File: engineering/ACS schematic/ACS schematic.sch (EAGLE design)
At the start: 4 parts

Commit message: schematics & engineering
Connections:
- net N$6 renamed W1
- net N$8 renamed W0
- removed net N$4: B1.GND@0, MCP41010.B0, MCP41010.B1, MCP41010.GND
- removed net N$5: B1.5V, MCP41010.A0, MCP41010.A1, MCP41010.VCC
- net GND: now also B1.GND@0, MCP41010.B0, MCP41010.B1, MCP41010.GND
- net VCC: now also B1.5V, MCP41010.A0, MCP41010.A1, MCP41010.VCC
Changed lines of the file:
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@@
 <plain>
 <text x="68.58" y="15.24" size="1.778" layer="91">MCP41010</text>
-<text x="30.48" y="10.16" size="1.778" layer="101">MC</text>
-<text x="30.48" y="0" size="1.778" layer="101">MC</text>
-<polygon width="0.1524" layer="208" spacing="76.2" pour="hatch">
-<vertex x="27.94" y="12.7"/>
-<vertex x="27.94" y="7.62"/>
-<vertex x="35.56" y="7.62"/>
-<vertex x="35.56" y="12.7"/>
-</polygon>
-<polygon width="0.1524" layer="208" spacing="76.2" pour="hatch">
-<vertex x="27.94" y="2.54"/>
-<vertex x="27.94" y="-2.54"/>
-<vertex x="35.56" y="-2.54"/>
-<vertex x="35.56" y="2.54"/>
-</polygon>
+<text x="30.48" y="10.16" size="1.778" layer="91">MC</text>
+<text x="30.48" y="0" size="1.778" layer="91">MC</text>
 </plain>
 <instances>
 <instance part="B1" gate="G$1" x="27.94" y="48.26"/>
-<instance part="MCP41010" gate="G$1" x="73.66" y="50.8">
-<attribute name="MCP41010" x="73.66" y="50.8" size="1.778" layer="96" display="off"/>
+<instance part="MCP41010" gate="G$1" x="73.66" y="48.26">
+<attribute name="MCP41010" x="73.66" y="48.26" size="1.778" layer="96" display="off"/>
 </instance>
 <instance part="SUPPLY1" gate="G$1" x="7.62" y="40.64"/>
@@
 </busses>
 <nets>
-<net name="N$5" class="0">
-<segment>
-<wire x1="10.16" y1="71.12" x2="53.34" y2="71.12" width="0.1524" layer="91"/>
-<pinref part="MCP41010" gate="G$1" pin="VCC"/>
-<junction x="63.5" y="68.58"/>
-<wire x1="53.34" y1="71.12" x2="58.42" y2="71.12" width="0.1524" layer="91"/>
-<wire x1="58.42" y1="71.12" x2="63.5" y2="71.12" width="0.1524" layer="91"/>
-<wire x1="63.5" y1="71.12" x2="63.5" y2="68.58" width="0.1524" layer="91"/>
-<pinref part="MCP41010" gate="G$1" pin="A1"/>
-<wire x1="63.5" y1="50.8" x2="53.34" y2="60.96" width="0.1524" layer="91"/>
-<wire x1="53.34" y1="60.96" x2="53.34" y2="71.12" width="0.1524" layer="91"/>
-<junction x="53.34" y="71.12"/>
-<pinref part="MCP41010" gate="G$1" pin="A0"/>
-<wire x1="63.5" y1="60.96" x2="58.42" y2="66.04" width="0.1524" layer="91"/>
-<wire x1="58.42" y1="66.04" x2="58.42" y2="71.12" width="0.1524" layer="91"/>
-<junction x="58.42" y="71.12"/>
-<pinref part="B1" gate="G$1" pin="5V"/>
-<wire x1="15.24" y1="38.1" x2="10.16" y2="38.1" width="0.1524" layer="91"/>
-<wire x1="10.16" y1="38.1" x2="10.16" y2="71.12" width="0.1524" layer="91"/>
-</segment>
-</net>
-<net name="N$4" class="0">
-<segment>
-<pinref part="MCP41010" gate="G$1" pin="GND"/>
-<wire x1="63.5" y1="20.32" x2="60.96" y2="20.32" width="0.1524" layer="91"/>
-<wire x1="60.96" y1="20.32" x2="55.88" y2="20.32" width="0.1524" layer="91"/>
-<pinref part="MCP41010" gate="G$1" pin="B0"/>
-<wire x1="63.5" y1="55.88" x2="60.96" y2="53.34" width="0.1524" layer="91"/>
-<wire x1="60.96" y1="53.34" x2="60.96" y2="20.32" width="0.1524" layer="91"/>
-<junction x="60.96" y="20.32"/>
-<pinref part="MCP41010" gate="G$1" pin="B1"/>
-<wire x1="63.5" y1="45.72" x2="55.88" y2="38.1" width="0.1524" layer="91"/>
-<wire x1="55.88" y1="38.1" x2="55.88" y2="20.32" width="0.1524" layer="91"/>
-<pinref part="B1" gate="G$1" pin="GND@0"/>
-<wire x1="15.24" y1="25.4" x2="15.24" y2="20.32" width="0.1524" layer="91"/>
-<wire x1="15.24" y1="20.32" x2="55.88" y2="20.32" width="0.1524" layer="91"/>
-<junction x="55.88" y="20.32"/>
-</segment>
-</net>
 <net name="N$1" class="0">
 <segment>
+<pinref part="B1" gate="G$1" pin="D13"/>
+<wire x1="50.8" y1="38.1" x2="50.8" y2="30.48" width="0.1524" layer="91"/>
+<wire x1="50.8" y1="30.48" x2="40.64" y2="30.48" width="0.1524" layer="91"/>
 <pinref part="MCP41010" gate="G$1" pin="SCK"/>
-<wire x1="63.5" y1="40.64" x2="50.8" y2="40.64" width="0.1524" layer="91"/>
-<wire x1="50.8" y1="40.64" x2="50.8" y2="30.48" width="0.1524" layer="91"/>
-<pinref part="B1" gate="G$1" pin="D13"/>
-<wire x1="50.8" y1="30.48" x2="40.64" y2="30.48" width="0.1524" layer="91"/>
-</segment>
-</net>
-<net name="N$2" class="0">
-<segment>
-<pinref part="MCP41010" gate="G$1" pin="DI"/>
-<pinref part="B1" gate="G$1" pin="*D11"/>
-<wire x1="63.5" y1="38.1" x2="48.26" y2="38.1" width="0.1524" layer="91"/>
-<wire x1="48.26" y1="38.1" x2="40.64" y2="35.56" width="0.1524" layer="91"/>
-</segment>
-</net>
-<net name="N$3" class="0">
-<segment>
-<pinref part="MCP41010" gate="G$1" pin="DO"/>
-<pinref part="B1" gate="G$1" pin="D12"/>
-<wire x1="63.5" y1="35.56" x2="48.26" y2="35.56" width="0.1524" layer="91"/>
-<wire x1="48.26" y1="35.56" x2="40.64" y2="33.02" width="0.1524" layer="91"/>
+<wire x1="63.5" y1="38.1" x2="50.8" y2="38.1" width="0.1524" layer="91"/>
 </segment>
 </net>
@@
 <wire x1="7.62" y1="40.64" x2="15.24" y2="40.64" width="0.1524" layer="91"/>
 </segment>
+<segment>
+<wire x1="10.16" y1="71.12" x2="53.34" y2="71.12" width="0.1524" layer="91"/>
+<pinref part="MCP41010" gate="G$1" pin="VCC"/>
+<junction x="63.5" y="66.04"/>
+<wire x1="53.34" y1="71.12" x2="58.42" y2="71.12" width="0.1524" layer="91"/>
+<wire x1="58.42" y1="71.12" x2="63.5" y2="71.12" width="0.1524" layer="91"/>
+<wire x1="63.5" y1="71.12" x2="63.5" y2="66.04" width="0.1524" layer="91"/>
+<pinref part="MCP41010" gate="G$1" pin="A1"/>
+<wire x1="63.5" y1="48.26" x2="53.34" y2="60.96" width="0.1524" layer="91"/>
+<wire x1="53.34" y1="60.96" x2="53.34" y2="71.12" width="0.1524" layer="91"/>
+<junction x="53.34" y="71.12"/>
+<pinref part="MCP41010" gate="G$1" pin="A0"/>
+<wire x1="63.5" y1="58.42" x2="58.42" y2="66.04" width="0.1524" layer="91"/>
+<wire x1="58.42" y1="66.04" x2="58.42" y2="71.12" width="0.1524" layer="91"/>
+<junction x="58.42" y="71.12"/>
+<pinref part="B1" gate="G$1" pin="5V"/>
+<wire x1="15.24" y1="38.1" x2="10.16" y2="38.1" width="0.1524" layer="91"/>
+<wire x1="10.16" y1="38.1" x2="10.16" y2="71.12" width="0.1524" layer="91"/>
+<label x="27.94" y="71.12" size="1.778" layer="95"/>
+</segment>
 </net>
 <net name="GND" class="0">
@@
 <wire x1="7.62" y1="30.48" x2="15.24" y2="30.48" width="0.1524" layer="91"/>
 </segment>
+<segment>
+<wire x1="60.96" y1="20.32" x2="55.88" y2="20.32" width="0.1524" layer="91"/>
+<pinref part="MCP41010" gate="G$1" pin="B0"/>
+<wire x1="63.5" y1="53.34" x2="60.96" y2="53.34" width="0.1524" layer="91"/>
+<wire x1="60.96" y1="53.34" x2="60.96" y2="20.32" width="0.1524" layer="91"/>
+<wire x1="55.88" y1="43.18" x2="55.88" y2="20.32" width="0.1524" layer="91"/>
+<pinref part="B1" gate="G$1" pin="GND@0"/>
+<wire x1="15.24" y1="25.4" x2="15.24" y2="20.32" width="0.1524" layer="91"/>
+<wire x1="15.24" y1="20.32" x2="55.88" y2="20.32" width="0.1524" layer="91"/>
+<junction x="55.88" y="20.32"/>
+<pinref part="MCP41010" gate="G$1" pin="GND"/>
+<wire x1="63.5" y1="17.78" x2="60.96" y2="17.78" width="0.1524" layer="91"/>
+<wire x1="60.96" y1="17.78" x2="60.96" y2="20.32" width="0.1524" layer="91"/>
+<junction x="60.96" y="20.32"/>
+<pinref part="MCP41010" gate="G$1" pin="B1"/>
+<wire x1="63.5" y1="43.18" x2="55.88" y2="43.18" width="0.1524" layer="91"/>
+<label x="60.96" y="15.24" size="1.778" layer="95"/>
+</segment>
 </net>
-<net name="N$8" class="0">
+<net name="W0" class="0">
 <segment>
-<pinref part="MCP41010" gate="G$1" pin="W0"/>
-<wire x1="63.5" y1="58.42" x2="58.42" y2="58.42" width="0.1524" layer="91"/>
 <pinref part="S2" gate="1" pin="P"/>
 <wire x1="53.34" y1="12.7" x2="58.42" y2="12.7" width="0.1524" layer="91"/>
-<wire x1="58.42" y1="12.7" x2="58.42" y2="58.42" width="0.1524" layer="91"/>
+<pinref part="MCP41010" gate="G$1" pin="W0"/>
+<wire x1="63.5" y1="55.88" x2="58.42" y2="55.88" width="0.1524" layer="91"/>
+<wire x1="58.42" y1="55.88" x2="58.42" y2="12.7" width="0.1524" layer="91"/>
+<label x="55.88" y="12.7" size="1.778" layer="95"/>
 </segment>
 </net>
-<net name="N$6" class="0">
+<net name="W1" class="0">
 <segment>
+<pinref part="S1" gate="1" pin="P"/>
 <pinref part="MCP41010" gate="G$1" pin="W1"/>
-<wire x1="63.5" y1="48.26" x2="53.34" y2="48.26" width="0.1524" layer="91"/>
-<pinref part="S1" gate="1" pin="P"/>
-<wire x1="53.34" y1="48.26" x2="53.34" y2="2.54" width="0.1524" layer="91"/>
+<wire x1="53.34" y1="45.72" x2="53.34" y2="2.54" width="0.1524" layer="91"/>
+<wire x1="63.5" y1="45.72" x2="53.34" y2="45.72" width="0.1524" layer="91"/>
+<label x="53.34" y="5.08" size="1.778" layer="95"/>
 </segment>
 </net>
@@
 </segment>
 </net>
+<net name="N$2" class="0">
+<segment>
+<pinref part="MCP41010" gate="G$1" pin="DI"/>
+<pinref part="B1" gate="G$1" pin="*D11"/>
+<wire x1="63.5" y1="35.56" x2="40.64" y2="35.56" width="0.1524" layer="91"/>
+</segment>
+</net>
+<net name="N$3" class="0">
+<segment>
+<pinref part="MCP41010" gate="G$1" pin="DO"/>
+<pinref part="B1" gate="G$1" pin="D12"/>
+<wire x1="63.5" y1="33.02" x2="40.64" y2="33.02" width="0.1524" layer="91"/>
+</segment>
+</net>

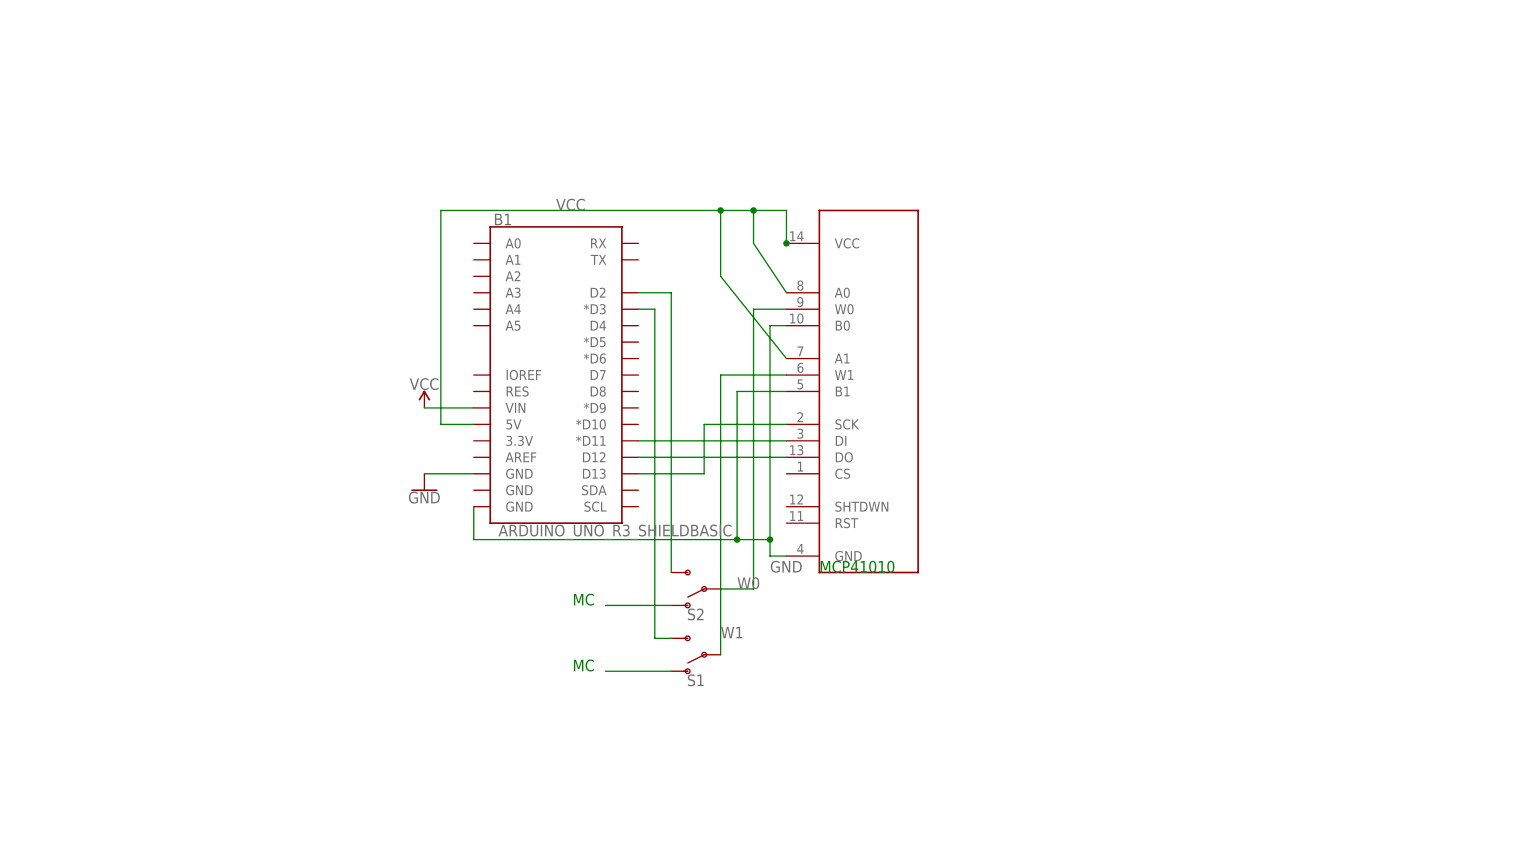
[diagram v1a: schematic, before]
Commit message: recorder added, steering training changes, config stuff added, other small changes
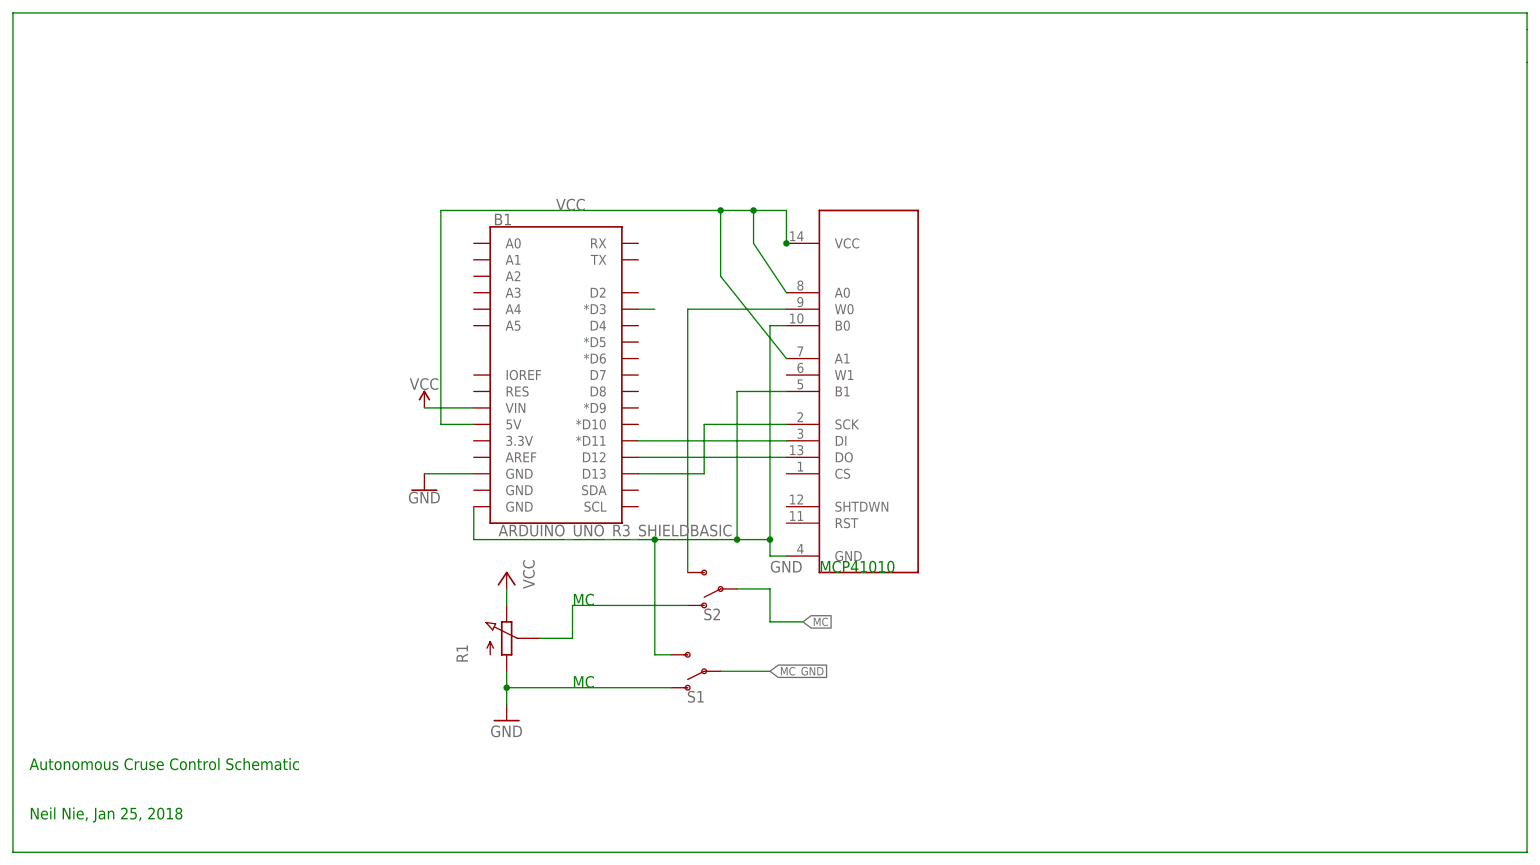
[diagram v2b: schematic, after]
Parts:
- added R1: (no value), pot-vitrohm:PC25
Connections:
- removed net N$11: S1.O
- removed net N$7: B1.D2, S2.S
- removed net W1: MCP41010.W1, S1.P
- new net MC: S2.P
- new net MC_GND: S1.P
- net GND: now also R1.A, S1.O, S1.S
- net N$10: now also R1.S
- net N$9: no longer S1.S
- net VCC: now also R1.E
- net W0: now also S2.S; no longer S2.P
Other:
- note added: "Autonomous Cruse Control Schematic"
- note added: "Neil Nie, Jan 25, 2018"
- moved on the sheet: S1, S2
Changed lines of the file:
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@@
 <?xml version="1.0" encoding="utf-8"?>
 <!DOCTYPE eagle SYSTEM "eagle.dtd">
-<eagle version="8.5.2">
+<eagle version="8.6.0">
 <drawing>
 <settings>
@@
 <part name="S1" library="SparkFun-Switches" library_urn="urn:adsk.eagle:library:535" deviceset="SWITCH-SPDT" device="-PTH-11.6X4.0MM" package3d_urn="urn:adsk.eagle:package:40177/1"/>
 <part name="S2" library="SparkFun-Switches" library_urn="urn:adsk.eagle:library:535" deviceset="SWITCH-SPDT" device="-PTH-11.6X4.0MM" package3d_urn="urn:adsk.eagle:package:40177/1"/>
+<part name="R1" library="pot-vitrohm" library_urn="urn:adsk.eagle:library:329" deviceset="PC25" device="" package3d_urn="urn:adsk.eagle:package:22616/1"/>
+<part name="GND2" library="supply1" library_urn="urn:adsk.eagle:library:371" deviceset="GND" device=""/>
+<part name="P+1" library="supply1" library_urn="urn:adsk.eagle:library:371" deviceset="VCC" device=""/>
 </parts>
 <sheets>
@@
 <text x="68.58" y="15.24" size="1.778" layer="91">MCP41010</text>
 <text x="30.48" y="10.16" size="1.778" layer="91">MC</text>
-<text x="30.48" y="0" size="1.778" layer="91">MC</text>
+<text x="30.48" y="-2.54" size="1.778" layer="91">MC</text>
+<text x="-53.34" y="-15.24" size="1.778" layer="91">Autonomous Cruse Control Schematic</text>
+<text x="-53.34" y="-22.86" size="1.778" layer="91">Neil Nie, Jan 25, 2018</text>
 </plain>
 <instances>
@@
 <instance part="SUPPLY1" gate="G$1" x="7.62" y="40.64"/>
 <instance part="GND1" gate="1" x="7.62" y="27.94"/>
-<instance part="S1" gate="1" x="50.8" y="2.54" rot="R180"/>
-<instance part="S2" gate="1" x="50.8" y="12.7" rot="R180"/>
+<instance part="S1" gate="1" x="50.8" y="0" rot="R180"/>
+<instance part="S2" gate="1" x="53.34" y="12.7" rot="R180"/>
+<instance part="R1" gate="G" x="20.32" y="5.08"/>
+<instance part="GND2" gate="1" x="20.32" y="-7.62"/>
+<instance part="P+1" gate="VCC" x="20.32" y="15.24" rot="MR0"/>
 </instances>
 <busses>
@@
 <label x="27.94" y="71.12" size="1.778" layer="95"/>
 </segment>
+<segment>
+<pinref part="R1" gate="G" pin="E"/>
+<pinref part="P+1" gate="VCC" pin="VCC"/>
+<wire x1="20.32" y1="10.16" x2="20.32" y2="12.7" width="0.1524" layer="91"/>
+</segment>
 </net>
 <net name="GND" class="0">
@@
 <pinref part="B1" gate="G$1" pin="GND@0"/>
 <wire x1="15.24" y1="25.4" x2="15.24" y2="20.32" width="0.1524" layer="91"/>
-<wire x1="15.24" y1="20.32" x2="55.88" y2="20.32" width="0.1524" layer="91"/>
+<wire x1="15.24" y1="20.32" x2="43.18" y2="20.32" width="0.1524" layer="91"/>
 <junction x="55.88" y="20.32"/>
 <pinref part="MCP41010" gate="G$1" pin="GND"/>
+<wire x1="43.18" y1="20.32" x2="55.88" y2="20.32" width="0.1524" layer="91"/>
 <wire x1="63.5" y1="17.78" x2="60.96" y2="17.78" width="0.1524" layer="91"/>
 <wire x1="60.96" y1="17.78" x2="60.96" y2="20.32" width="0.1524" layer="91"/>
@@
 <wire x1="63.5" y1="43.18" x2="55.88" y2="43.18" width="0.1524" layer="91"/>
 <label x="60.96" y="15.24" size="1.778" layer="95"/>
+<pinref part="S1" gate="1" pin="S"/>
+<wire x1="45.72" y1="2.54" x2="43.18" y2="2.54" width="0.1524" layer="91"/>
+<wire x1="43.18" y1="2.54" x2="43.18" y2="20.32" width="0.1524" layer="91"/>
+<junction x="43.18" y="20.32"/>
+</segment>
+<segment>
+<pinref part="R1" gate="G" pin="A"/>
+<pinref part="GND2" gate="1" pin="GND"/>
+<wire x1="20.32" y1="0" x2="20.32" y2="-2.54" width="0.1524" layer="91"/>
+<pinref part="S1" gate="1" pin="O"/>
+<wire x1="20.32" y1="-2.54" x2="20.32" y2="-5.08" width="0.1524" layer="91"/>
+<wire x1="45.72" y1="-2.54" x2="20.32" y2="-2.54" width="0.1524" layer="91"/>
+<junction x="20.32" y="-2.54"/>
 </segment>
 </net>
 <net name="W0" class="0">
 <segment>
-<pinref part="S2" gate="1" pin="P"/>
-<wire x1="53.34" y1="12.7" x2="58.42" y2="12.7" width="0.1524" layer="91"/>
 <pinref part="MCP41010" gate="G$1" pin="W0"/>
-<wire x1="63.5" y1="55.88" x2="58.42" y2="55.88" width="0.1524" layer="91"/>
-<wire x1="58.42" y1="55.88" x2="58.42" y2="12.7" width="0.1524" layer="91"/>
-<label x="55.88" y="12.7" size="1.778" layer="95"/>
-</segment>
-</net>
-<net name="W1" class="0">
-<segment>
-<pinref part="S1" gate="1" pin="P"/>
-<pinref part="MCP41010" gate="G$1" pin="W1"/>
-<wire x1="53.34" y1="45.72" x2="53.34" y2="2.54" width="0.1524" layer="91"/>
-<wire x1="63.5" y1="45.72" x2="53.34" y2="45.72" width="0.1524" layer="91"/>
-<label x="53.34" y="5.08" size="1.778" layer="95"/>
-</segment>
-</net>
-<net name="N$7" class="0">
-<segment>
-<pinref part="B1" gate="G$1" pin="D2"/>
-<wire x1="40.64" y1="58.42" x2="45.72" y2="58.42" width="0.1524" layer="91"/>
 <pinref part="S2" gate="1" pin="S"/>
-<wire x1="45.72" y1="58.42" x2="45.72" y2="15.24" width="0.1524" layer="91"/>
+<wire x1="48.26" y1="15.24" x2="48.26" y2="55.88" width="0.1524" layer="91"/>
+<wire x1="48.26" y1="55.88" x2="63.5" y2="55.88" width="0.1524" layer="91"/>
 </segment>
 </net>
 <net name="N$9" class="0">
 <segment>
-<pinref part="S1" gate="1" pin="S"/>
-<wire x1="45.72" y1="5.08" x2="43.18" y2="5.08" width="0.1524" layer="91"/>
-<wire x1="43.18" y1="5.08" x2="43.18" y2="55.88" width="0.1524" layer="91"/>
 <pinref part="B1" gate="G$1" pin="*D3"/>
 <wire x1="43.18" y1="55.88" x2="40.64" y2="55.88" width="0.1524" layer="91"/>
@@
 <segment>
 <pinref part="S2" gate="1" pin="O"/>
-<wire x1="45.72" y1="10.16" x2="35.56" y2="10.16" width="0.1524" layer="91"/>
-</segment>
-</net>
-<net name="N$11" class="0">
-<segment>
-<pinref part="S1" gate="1" pin="O"/>
-<wire x1="45.72" y1="0" x2="35.56" y2="0" width="0.1524" layer="91"/>
+<wire x1="48.26" y1="10.16" x2="30.48" y2="10.16" width="0.1524" layer="91"/>
+<pinref part="R1" gate="G" pin="S"/>
+<wire x1="25.4" y1="5.08" x2="30.48" y2="5.08" width="0.1524" layer="91"/>
+<wire x1="30.48" y1="5.08" x2="30.48" y2="10.16" width="0.1524" layer="91"/>
 </segment>
 </net>
@@
 </segment>
 </net>
+<net name="N$4" class="0">
+<segment>
+<wire x1="177.8" y1="99.06" x2="177.8" y2="93.98" width="0.1524" layer="91"/>
+<wire x1="177.8" y1="93.98" x2="177.8" y2="-27.94" width="0.1524" layer="91"/>
+<wire x1="-55.88" y1="-27.94" x2="-55.88" y2="101.6" width="0.1524" layer="91"/>
+<wire x1="-55.88" y1="-27.94" x2="177.8" y2="-27.94" width="0.1524" layer="91"/>
+<wire x1="-55.88" y1="101.6" x2="177.8" y2="101.6" width="0.1524" layer="91"/>
+<wire x1="177.8" y1="101.6" x2="177.8" y2="99.06" width="0.1524" layer="91"/>
+</segment>
+</net>
+<net name="MC" class="0">
+<segment>
+<pinref part="S2" gate="1" pin="P"/>
+<wire x1="55.88" y1="12.7" x2="60.96" y2="12.7" width="0.1524" layer="91"/>
+<wire x1="60.96" y1="12.7" x2="60.96" y2="7.62" width="0.1524" layer="91"/>
+<wire x1="60.96" y1="7.62" x2="66.04" y2="7.62" width="0.1524" layer="91"/>
+<label x="66.04" y="7.62" size="1.27" layer="95" xref="yes"/>
+</segment>
+</net>
+<net name="MC_GND" class="0">
+<segment>
+<pinref part="S1" gate="1" pin="P"/>
+<wire x1="53.34" y1="0" x2="60.96" y2="0" width="0.1524" layer="91"/>
+<label x="60.96" y="0" size="1.27" layer="95" xref="yes"/>
+</segment>
+</net>
